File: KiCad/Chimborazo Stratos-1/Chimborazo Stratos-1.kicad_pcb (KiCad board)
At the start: 2 copper layers, 90 x 90 mm, 7 parts, among them J1 BMP280, J2 MPU6050, J3 Conn_01x03_Pin, J4 Conn_01x03_Pin, U1 XIAO-RP2040-DIP

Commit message: Final PCB done!
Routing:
- net VBUS: track 67.0 -> 92.9 mm, vias 0 -> 1
- net (no net): vias 0 -> 6
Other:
- board text added: "By Cocotrilo"
- board text added: "Chimborazo Stratos-1"

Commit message: New PCB OF 45mm Diameter finished :)
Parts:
- added REF**: MountingHole_3.2mm_M3, MountingHole:MountingHole_3.2mm_M3, F.Cu at (158.0, 129.5)
- added REF**: MountingHole_3.2mm_M3, MountingHole:MountingHole_3.2mm_M3, F.Cu at (121.5, 67.7)
- added REF**: MountingHole_3.2mm_M3, MountingHole:MountingHole_3.2mm_M3, F.Cu at (122.4, 129.5)
- added REF**: MountingHole_3.2mm_M3, MountingHole:MountingHole_3.2mm_M3, F.Cu at (159.5, 68.0)
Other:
- board size 90 x 90 mm -> 45 x 46 mm

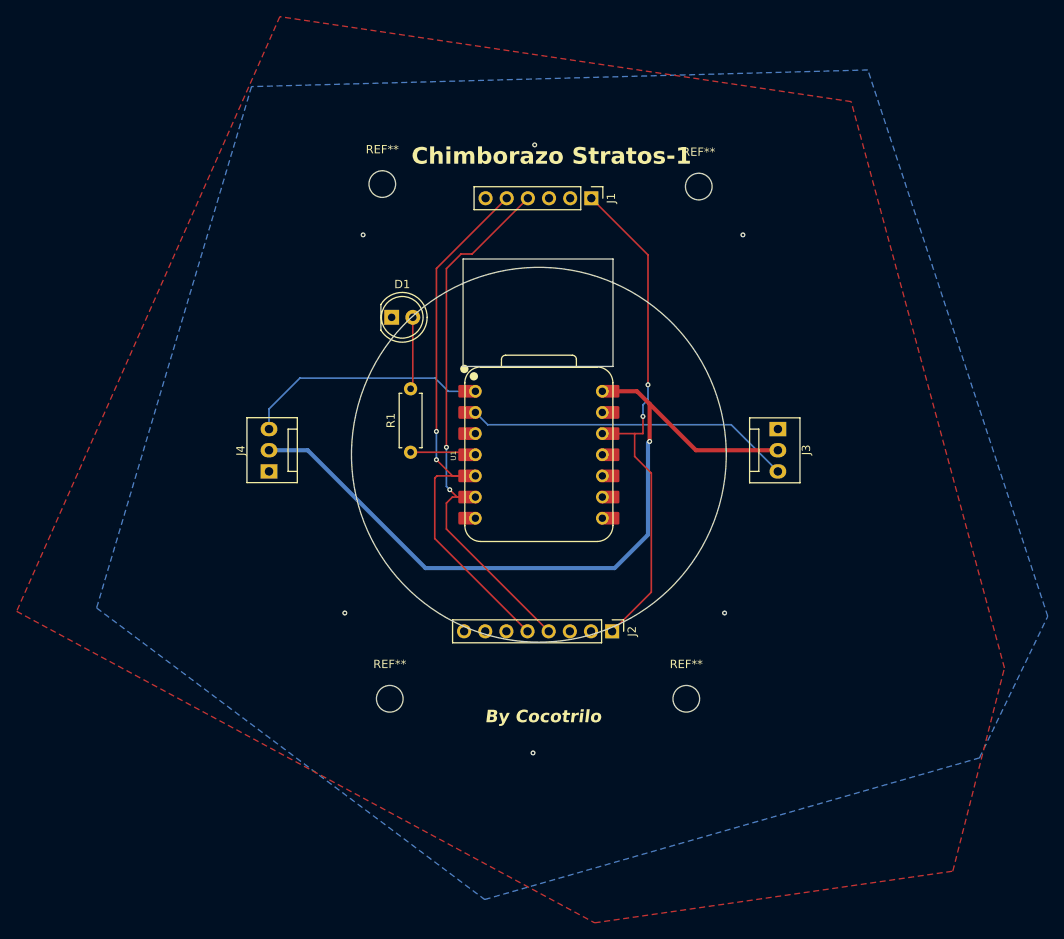
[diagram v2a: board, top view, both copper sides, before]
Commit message: Re-work of pcb and CAD model
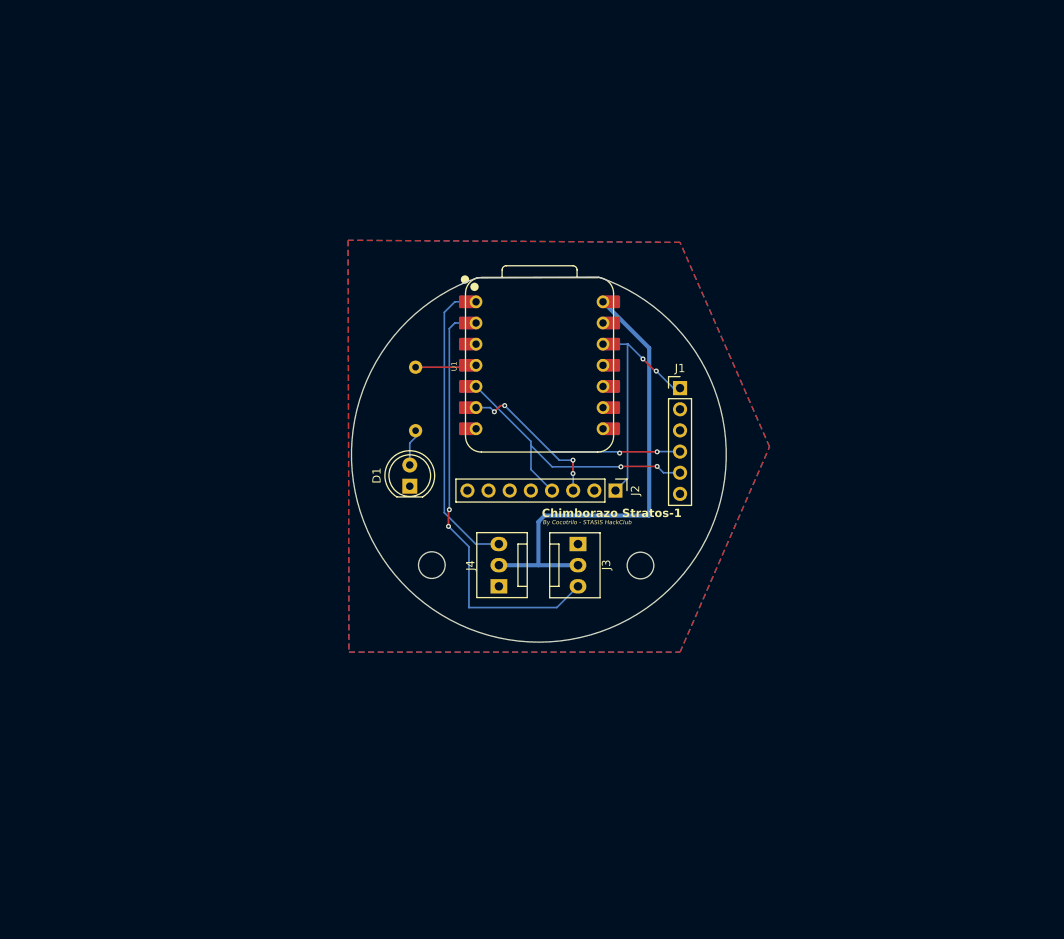
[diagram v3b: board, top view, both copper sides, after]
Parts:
- removed the REF** at (121.5, 67.7)
- removed the REF** at (159.5, 68.0)
- R1: moved to B.Cu
- moved J4 30.9 mm to (135.5, 116.0)
- moved J3 27.7 mm to (145.0, 110.9)
- moved J1 25.2 mm to (157.2, 92.2), turned to 0 degrees
- moved D1 20.4 mm to (124.8, 104.0), turned to 90 degrees
- moved REF** 16.9 mm to (152.5, 113.5)
- moved J2 16.9 mm to (149.5, 104.5)
- moved REF** 16.8 mm to (127.5, 113.5)
- moved U1 10.7 mm to (140.4, 89.5)
- moved R1 10.2 mm to (125.5, 89.7), turned to -90 degrees
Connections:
- net 3V3 renamed +3V3
- J2 pad 3: unconnected-(J2-Pin_3-Pad3) -> SCL
- J2 pad 4: SCL -> SDA
- J2 pad 5: SDA -> unconnected-(J2-Pin_5-Pad5)
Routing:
- net VBUS: track 92.9 -> 56.3 mm, vias 1 -> 0
- net +3V3: track 62.7 -> 29.6 mm
- net SCL: track 67.7 -> 35.2 mm, vias 2 -> 6
- net SDA: track 68.4 -> 36.6 mm
- net PWM_2: track 39.3 -> 52.3 mm, vias 0 -> 2
- net PWM_1: track 29.4 -> 37.6 mm
- net Net-(D1-A): track 8.69 -> 4.41 mm
- net (no net): vias 6 -> 0
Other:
- board size 45 x 46 mm -> 45 x 43.8 mm
- board text added: "By Cocotrilo - STASIS HackClub"
- board text removed: "By Cocotrilo"

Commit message: Finished the pcb and the cad model REAL NO FAKE
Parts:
- moved J2 28.2 mm to (126.2, 88.6), turned to 0 degrees
- moved D1 19.2 mm to (144.0, 105.1)
- moved R1 15.2 mm to (130.0, 104.2), turned to 0 degrees
- moved J3 9.50 mm to (135.5, 110.9)
- moved J4 9.50 mm to (145.0, 116.0)
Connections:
- J1 pad 3: unconnected-(J1-Pin_3-Pad3) -> SCL
- J1 pad 4: SCL -> SDA
- J1 pad 5: SDA -> unconnected-(J1-Pin_5-Pad5)
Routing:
- net Net-(U1-P29_A3_D3): track 7.68 -> 17.1 mm
- net PWM_1: track 37.6 -> 46.4 mm, vias 0 -> 4
- net +3V3: track 29.6 -> 36.2 mm
- net PWM_2: track 52.3 -> 57.9 mm
- net SDA: track 36.6 -> 40.8 mm, vias 2 -> 4
- net Net-(D1-A): track 4.41 -> 7.01 mm
- net SCL: track 35.2 -> 36.1 mm, vias 6 -> 2

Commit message: Remade schmeatic changed components and Remade PCB with new and improved layout
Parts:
- removed J1: BMP280, Connector_PinHeader_2.54mm:PinHeader_1x06_P2.54mm_Vertical
- removed J2: MPU6050, Connector_PinHeader_2.54mm:PinHeader_1x08_P2.54mm_Vertical
- removed J3, J4: Conn_01x03_Pin, Connector:FanPinHeader_1x03_P2.54mm_Vertical
- removed REF** (x2): MountingHole_3.2mm_M3, MountingHole:MountingHole_3.2mm_M3
- added C2: 100nF, Capacitor_SMD:C_0805_2012Metric, F.Cu at (151.5, 86.9)
- added C5: 100nF, Capacitor_SMD:C_0805_2012Metric, F.Cu at (151.5, 83.1)
- added C6: 100nF, Capacitor_SMD:C_0805_2012Metric, F.Cu at (131.1, 103.6)
- added D2: LED, LED_SMD:LED_0805_2012Metric, F.Cu at (122.8, 108.5)
- added F1: Polyfuse, Fuse:Fuse_1206_3216Metric, F.Cu at (135.3, 104.6)
- added G***: LOGO, LOGO, F.Cu at (142.7, 97.6)
- added G***: LOGO, LOGO, B.Cu at (140.9, 100.8)
- added JBATTERY1: Conn_01x02, Connector_JST:JST_PH_B2B-PH-K_1x02_P2.00mm_Vertical, B.Cu at (139.9, 104.1)
- added JGPS1: Conn_01x04, Connector_PinHeader_2.54mm:PinHeader_1x04_P2.54mm_Vertical, F.Cu at (159.5, 94.8)
- added JGY1: Conn_01x10, Connector_PinHeader_2.54mm:PinHeader_1x10_P2.54mm_Vertical, F.Cu at (128.9, 116.5)
- added JPyro1: Conn_01x02_Socket, Connector_PinHeader_2.54mm:PinHeader_1x02_P2.54mm_Vertical, F.Cu at (126.4, 85.9)
- added Q1: AO3400A, Package_TO_SOT_SMD:SOT-23, F.Cu at (122.6, 92.5)
- added R2: R, Resistor_SMD:R_0805_2012Metric, F.Cu at (129.1, 105.9)
- added R3: 4.7k, Resistor_SMD:R_0805_2012Metric, F.Cu at (127.5, 95.6)
- added R4: 4.7k, Resistor_SMD:R_0805_2012Metric, F.Cu at (129.5, 95.6)
- added R5: 10k, Resistor_SMD:R_0805_2012Metric, F.Cu at (125.3, 93.7)
- added R6: 1k, Resistor_SMD:R_0805_2012Metric, F.Cu at (126.2, 110.8)
- added R7: 1k, Resistor_SMD:R_0805_2012Metric, F.Cu at (124.7, 107.6)
- added Servo1: Conn_01x03, Connector_PinHeader_2.54mm:PinHeader_1x03_P2.54mm_Vertical, B.Cu at (151.8, 101.4)
- added Servo2: Conn_01x03, Connector_PinHeader_2.54mm:PinHeader_1x03_P2.54mm_Vertical, B.Cu at (155.5, 101.5)
- D1: footprint LED_THT:LED_D5.0mm -> LED_SMD:LED_0805_2012Metric
- R1: value 220 -> 200k; footprint Resistor_THT:R_Axial_DIN0207_L6.3mm_D2.5mm_P7.62mm_Horizontal -> Resistor_SMD:R_0805_2012Metric; moved to F.Cu
- U1: value XIAO-RP2040-DIP -> XIAO-ESP32-C6-SMD; footprint Seeed Studio XIAO Series Library:XIAO-RP2040-DIP -> xiaoesp32c6:XIAO-ESP32-C6-SMD
- moved D1 20.8 mm to (124.3, 111.7), turned to 115 degrees
- moved U1 14.1 mm to (131.2, 100.1), turned to 0 degrees
- moved R1 3.06 mm to (133.1, 104.0), turned to -90 degrees
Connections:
- R1 pad 1: Net-(U1-P29_A3_D3) -> /VBAT
- R1 pad 2: Net-(D1-A) -> /BAT_SENSE
- U1 pad 1: PWM_1 -> /BAT_SENSE
- U1 pad 10: unconnected-(U1-P4_D9_MISO-Pad10)_1 -> /LED_ARMED
- U1 pad 11: unconnected-(U1-P3_D10_MOSI-Pad11) -> /LED_ERROR
- U1 pad 14: VBUS -> +5V
- U1 pad 2: PWM_2 -> /SERVO1
- U1 pad 3: unconnected-(U1-P28_A2_D2-Pad3) -> /SERVO2
- U1 pad 4: Net-(U1-P29_A3_D3) -> /PYRO_GATE
- U1 pad 5: SDA -> /SDA
- U1 pad 6: SCL -> /SCL
- U1 pad 7: unconnected-(U1-P0_D6_TX-Pad7)_1 -> /GPS_TX
- U1 pad 8: unconnected-(U1-P1_D7_RX-Pad8) -> /GPS_RX
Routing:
- net +3V3: track 36.2 -> 121.7 mm, vias 2 -> 3
- net PWM_2: track 57.9 -> 0.00 mm, vias 2 -> 0
- net VBUS: track 56.3 -> 0.00 mm
- net +5V: track 0.00 -> 53.9 mm, vias 0 -> 2
- net PWM_1: track 46.4 -> 0.00 mm, vias 4 -> 0
- net SDA: track 40.8 -> 0.00 mm, vias 4 -> 0
- net /LED_ARMED: track 0.00 -> 36.9 mm
- net /GPS_TX: track 0.00 -> 36.8 mm, vias 0 -> 2
- net SCL: track 36.1 -> 0.00 mm, vias 2 -> 0
- net /SDA: track 0.00 -> 35.0 mm, vias 0 -> 2
- net /SERVO1: track 0.00 -> 34.6 mm, vias 0 -> 2
- net /SERVO2: track 0.00 -> 34.5 mm, vias 0 -> 2
- net /LED_ERROR: track 0.00 -> 33.4 mm
- net /BAT_SENSE: track 0.00 -> 29.8 mm, vias 0 -> 2
- net /SCL: track 0.00 -> 29.2 mm, vias 0 -> 2
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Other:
- board text added: "By Cocotrilo"
- board text added: "STASIS - HackClub -"
- board text removed: "By Cocotrilo - STASIS HackClub"

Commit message: Added BOM firmware, CAD, Schematic update, and more Images
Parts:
- added REF**: MountingHole_3.2mm_M3, MountingHole:MountingHole_3.2mm_M3, F.Cu at (122.5, 100.2)
- added REF**: MountingHole_3.2mm_M3, MountingHole:MountingHole_3.2mm_M3, F.Cu at (149.2, 109.1)
- moved G*** 8.85 mm to (141.8, 109.6)
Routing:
- net /GPS_TX: track 36.8 -> 35.2 mm
